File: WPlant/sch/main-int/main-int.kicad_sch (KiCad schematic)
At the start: 63 parts, among them J1 PROG/JTAG, J10 Ext, J8 eInk-Buttons, J9 Leak, M1 Motor_DC, U1 SIWG917Y121MGABAR, U10 SP485EEN-L/TR, U11 TXU0102QDCURQ1, U5 TC4427AEOA713, U8 NC7S02P5, U9 INA180A2, X1 SIT1552AI-JE-DCC-32.768D

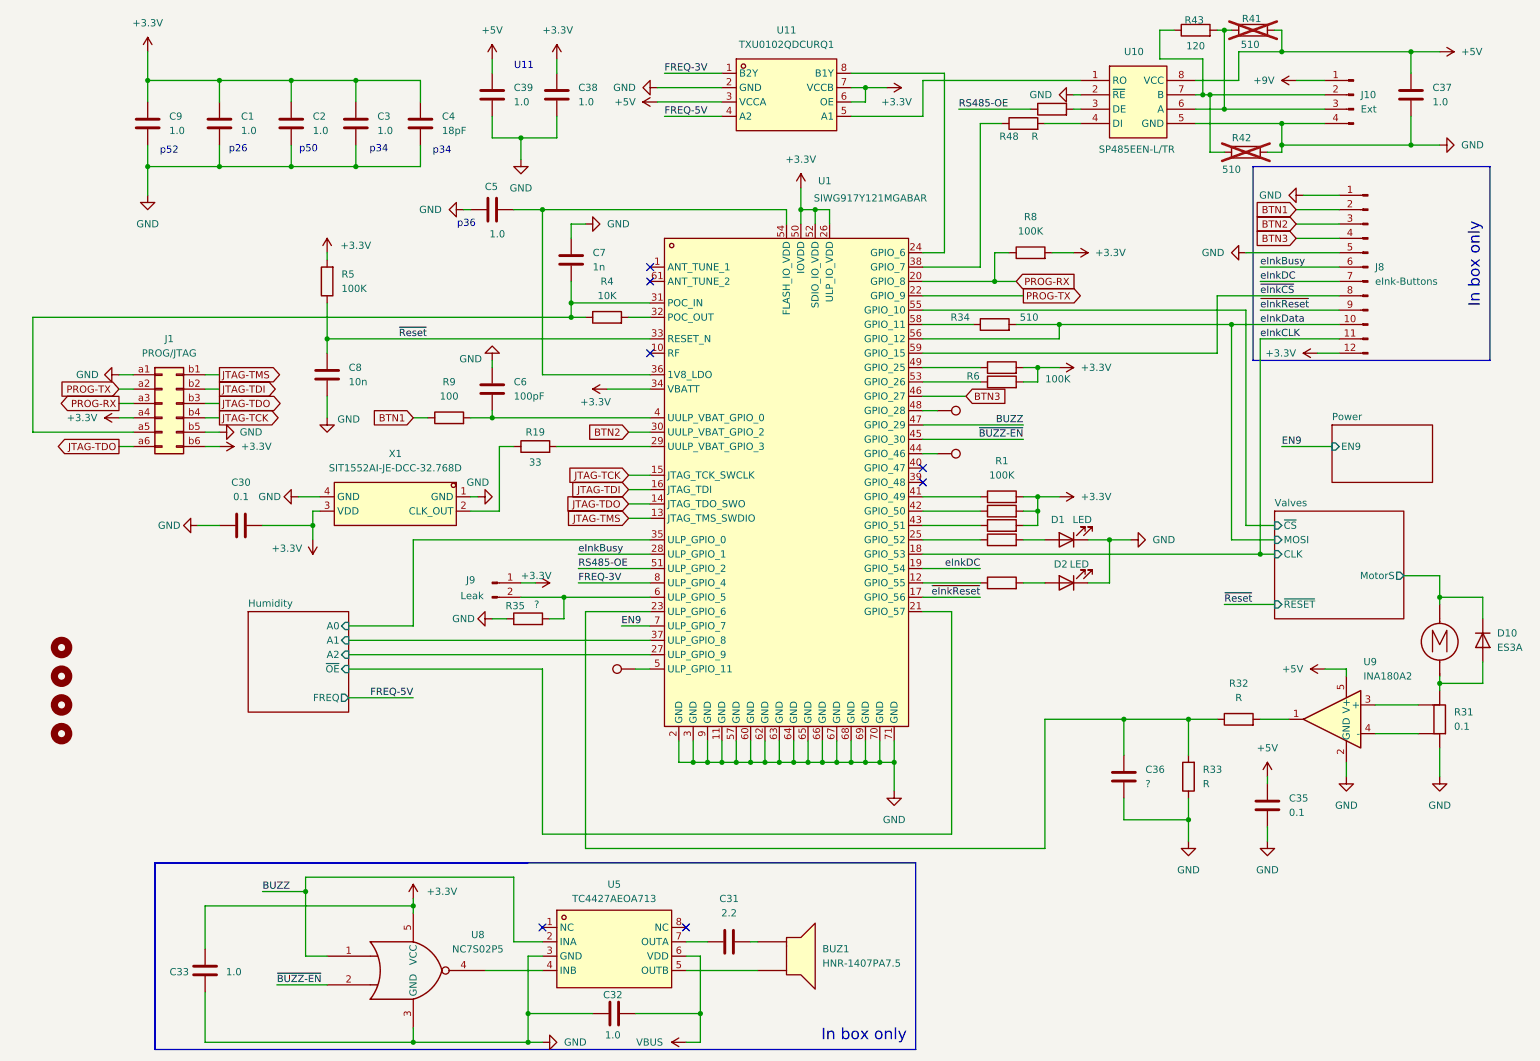
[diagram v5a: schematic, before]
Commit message: Upate values in SCH of WP
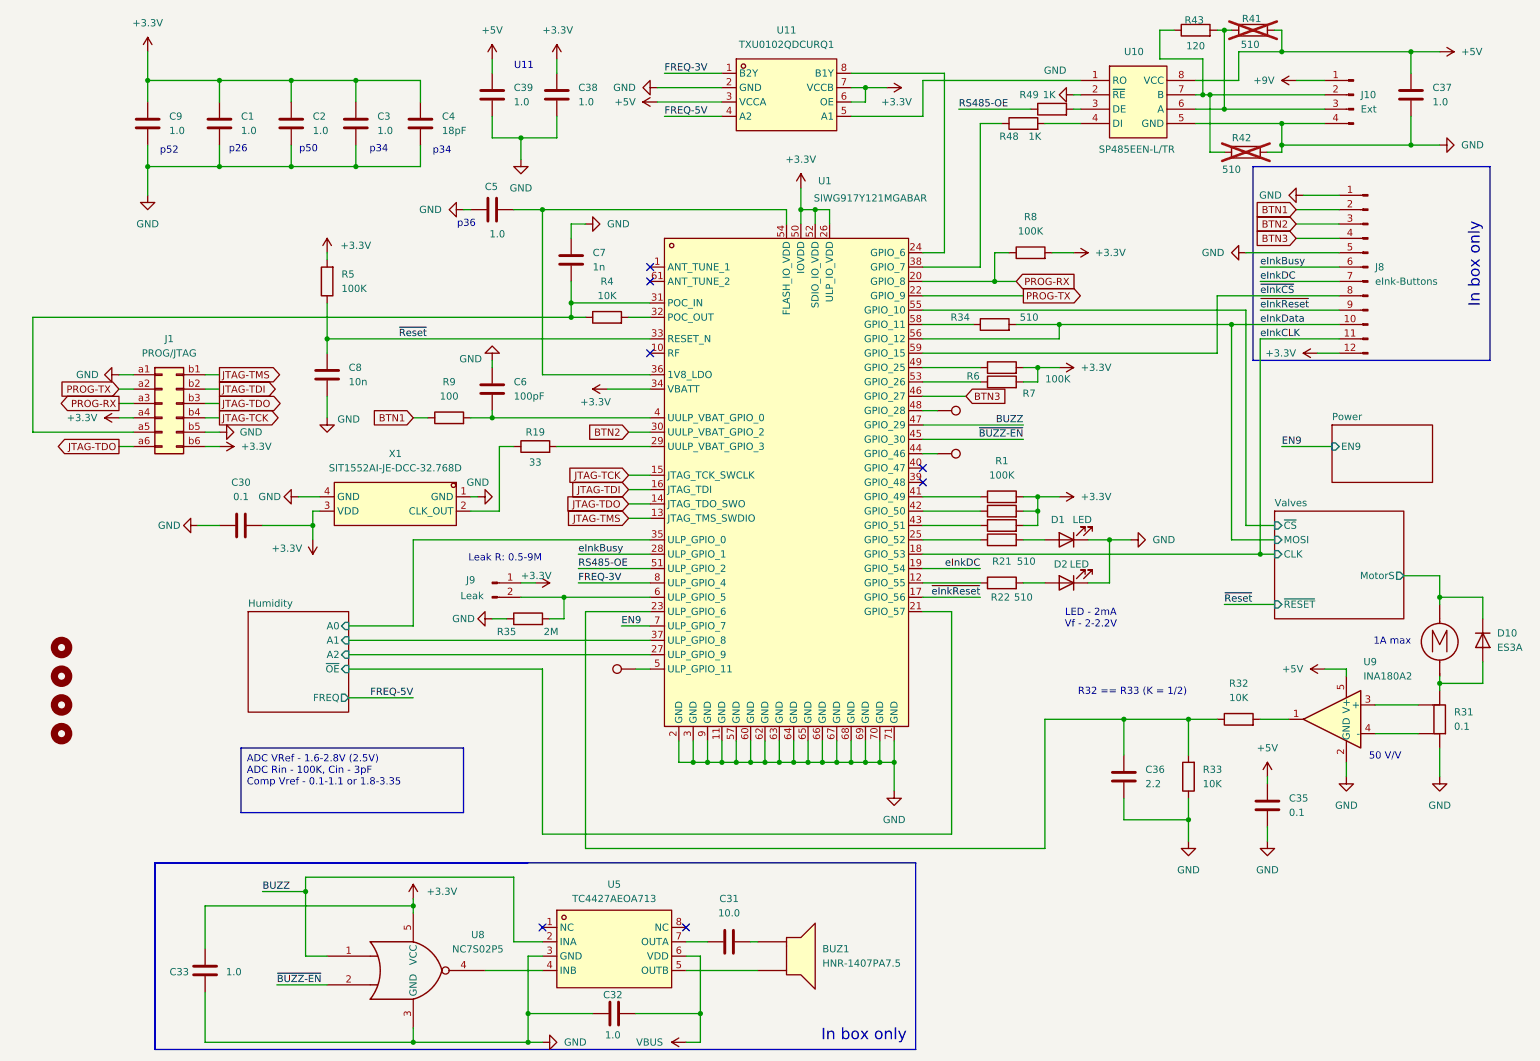
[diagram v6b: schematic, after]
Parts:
- C31: value 2.2 -> 10.0
- C36: value ? -> 2.2
- R21, R22: value 100K -> 510
- R32, R33: value R -> 10K
- R35: value ? -> 2M
- R48, R49: value R -> 1K
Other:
- note added: "1A max"
- note added: "50 V/V"
- note added: "LED - 2mA Vf - 2-2.2V"
- note added: "Leak R: 0.5-9M"
- note added: "R32 == R33 (K = 1/2)"
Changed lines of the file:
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@@
 		)
 	)
+	(text_box "ADC VRef - 1.6-2.8V (2.5V)\nADC Rin - 100K, Cin - 3pF\nComp Vref - 0.1-1.1 or 1.8-3.35\n"
+		(exclude_from_sim no)
+		(at 55.88 142.24 0)
+		(size 39.37 11.43)
+		(stroke
+			(width 0)
+			(type default)
+		)
+		(fill
+			(type none)
+		)
+		(effects
+			(font
+				(size 1.27 1.27)
+			)
+			(justify left top)
+		)
+	)
 	(text "p34"
 		(exclude_from_sim no)
@@
 		)
 	)
+	(text "1A max"
+		(exclude_from_sim no)
+		(at 259.588 123.444 0)
+		(effects
+			(font
+				(size 1.27 1.27)
+			)
+		)
+	)
 	(text "p36"
 		(exclude_from_sim no)
@@
 		)
 	)
+	(text "50 V/V"
+		(exclude_from_sim no)
+		(at 258.318 143.764 0)
+		(effects
+			(font
+				(size 1.27 1.27)
+			)
+		)
+	)
+	(text "R32 == R33 (K = 1/2)"
+		(exclude_from_sim no)
+		(at 213.614 132.334 0)
+		(effects
+			(font
+				(size 1.27 1.27)
+			)
+		)
+	)
 	(text "p34"
 		(exclude_from_sim no)
@@
 		)
 	)
+	(text "Leak R: 0.5-9M"
+		(exclude_from_sim no)
+		(at 102.616 108.712 0)
+		(effects
+			(font
+				(size 1.27 1.27)
+			)
+		)
+	)
 	(text "U11"
 		(exclude_from_sim no)
@@
 		)
 	)
+	(text "LED - 2mA\nVf - 2-2.2V"
+		(exclude_from_sim no)
+		(at 206.248 119.38 0)
+		(effects
+			(font
+				(size 1.27 1.27)
+			)
+		)
+	)
 	(text "p52"
 		(exclude_from_sim no)
@@
 		(on_board yes)
 		(dnp no)
-		(fields_autoplaced yes)
 		(property "Reference" "#PWR092"
 			(at 196.85 26.67 0)
@@
 		)
 		(property "Value" "GND"
-			(at 199.39 26.6699 90)
+			(at 201.93 22.352 90)
 			(effects
 				(font
@@
 		(dnp no)
 		(property "Reference" "R49"
-			(at 196.85 31.496 90)
+			(at 195.326 26.67 90)
 			(effects
 				(font
 					(size 1.27 1.27)
 				)
-				(hide yes)
 			)
 		)
-		(property "Value" "R"
-			(at 201.422 31.496 90)
+		(property "Value" "1K"
+			(at 198.882 26.67 90)
 			(effects
 				(font
 					(size 1.27 1.27)
 				)
-				(hide yes)
 			)
 		)
@@
 		(on_board yes)
 		(dnp no)
-		(fields_autoplaced yes)
 		(property "Reference" "R22"
-			(at 190.5 106.68 90)
+			(at 190.246 115.57 90)
 			(effects
 				(font
 					(size 1.27 1.27)
 				)
-				(hide yes)
 			)
 		)
-		(property "Value" "100K"
-			(at 190.5 109.22 90)
+		(property "Value" "510"
+			(at 194.31 115.57 90)
 			(effects
 				(font
 					(size 1.27 1.27)
 				)
-				(hide yes)
 			)
 		)
@@
 			)
 		)
-		(property "Value" "R"
+		(property "Value" "10K"
 			(at 226.06 148.5899 0)
 			(effects
@@
 		(on_board yes)
 		(dnp no)
-		(fields_autoplaced yes)
 		(property "Reference" "R21"
-			(at 190.5 99.06 90)
+			(at 190.5 109.22 90)
 			(effects
 				(font
 					(size 1.27 1.27)
 				)
-				(hide yes)
 			)
 		)
-		(property "Value" "100K"
-			(at 190.5 101.6 90)
+		(property "Value" "510"
+			(at 194.818 109.22 90)
 			(effects
 				(font
 					(size 1.27 1.27)
 				)
-				(hide yes)
 			)
 		)
@@
 			)
 		)
-		(property "Value" "R"
+		(property "Value" "1K"
 			(at 196.342 34.036 90)
 			(effects
@@
 		(dnp no)
 		(property "Reference" "R35"
-			(at 104.394 117.094 90)
+			(at 102.87 121.666 90)
 			(effects
 				(font
@@
 			)
 		)
-		(property "Value" "?"
-			(at 108.204 116.84 90)
+		(property "Value" "2M"
+			(at 110.744 121.666 90)
 			(effects
 				(font
@@
 			)
 		)
-		(property "Value" "R"
+		(property "Value" "10K"
 			(at 232.41 133.35 90)
 			(effects
@@
 			)
 		)
-		(property "Value" "?"
+		(property "Value" "2.2"
 			(at 215.9 148.5899 0)
 			(effects
@@
 			)
 		)
-		(property "Value" "2.2"
+		(property "Value" "10.0"
 			(at 142.24 171.45 90)
 			(effects
@@
 		(on_board yes)
 		(dnp no)
-		(fields_autoplaced yes)
 		(property "Reference" "R7"
-			(at 190.5 71.12 90)
+			(at 195.326 79.502 90)
 			(effects
 				(font
 					(size 1.27 1.27)
 				)
-				(hide yes)
 			)
 		)

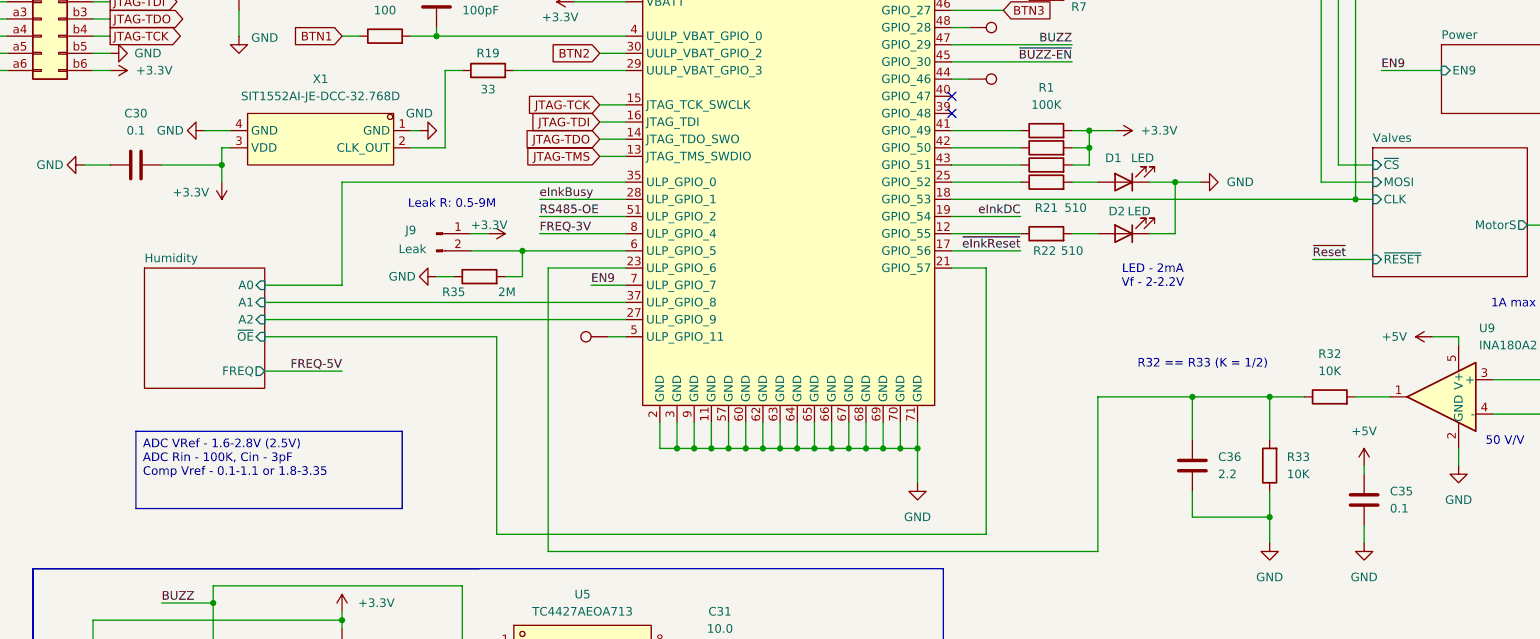
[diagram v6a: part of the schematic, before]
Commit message: Update WP Sch (sheets titles, replaced wires by bus, update components values)
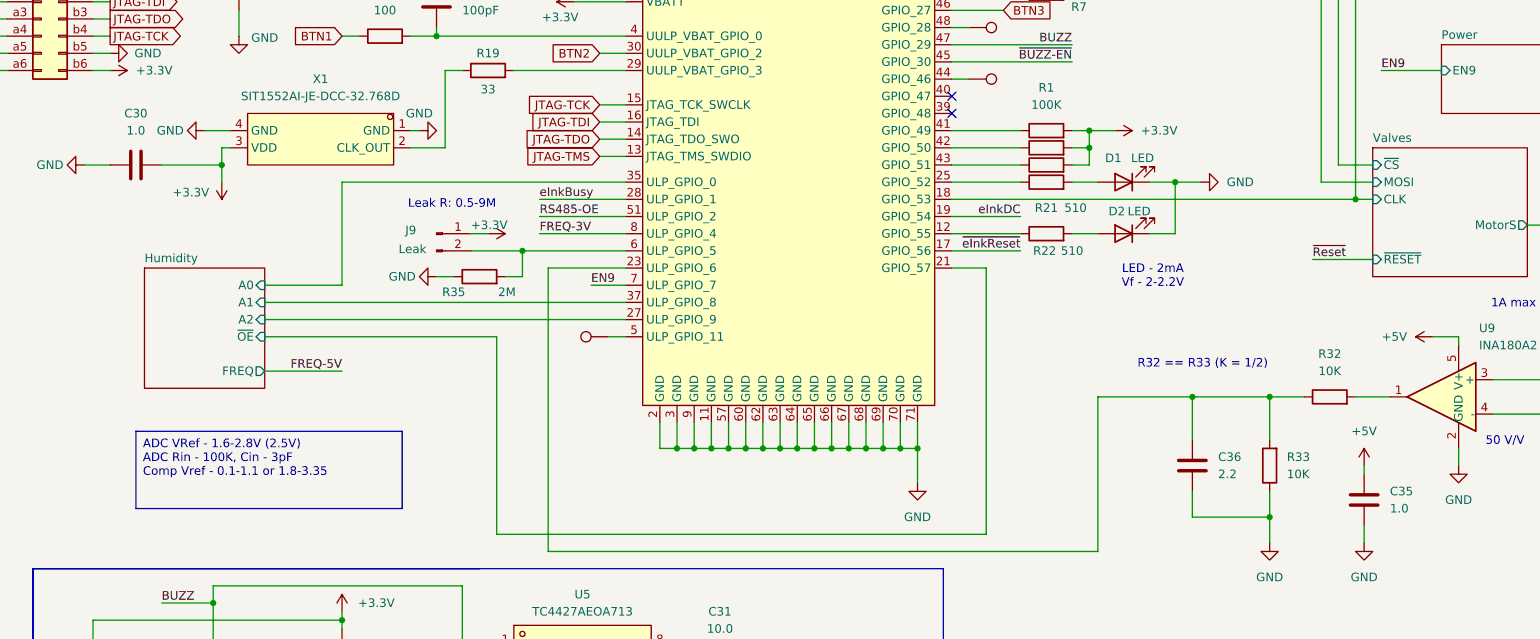
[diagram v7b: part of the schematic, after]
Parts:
- C30, C35: value 0.1 -> 1.0
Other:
- title: Water Plant main module -> Water Plant main module (Internal)
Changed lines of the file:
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@@
 	(paper "A4")
 	(title_block
-		(title "Water Plant main module")
+		(title "Water Plant main module (Internal)")
+		(date "2026-02-05")
 		(company "RoboWay")
 	)
@@
 			)
 		)
-		(property "Value" "0.1"
+		(property "Value" "1.0"
 			(at 55.88 97.79 90)
 			(effects
@@
 			)
 		)
-		(property "Value" "0.1"
+		(property "Value" "1.0"
 			(at 241.3 153.6699 0)
 			(effects
